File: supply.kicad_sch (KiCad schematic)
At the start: 98 parts, among them IC12 74HC00PW, IC13 SN74LVC1G126DCKR, IC4 TPS7A0518PDBVT, J12 533980471, T3 BSS138APW, U1 LM3671MF-3.3/NOPB, U2 LM62440-Q1, U3 SN74LXC1T45DBVR, U5 LM3671MF-3.3/NOPB, U6 SIC477ED-T1-GE3

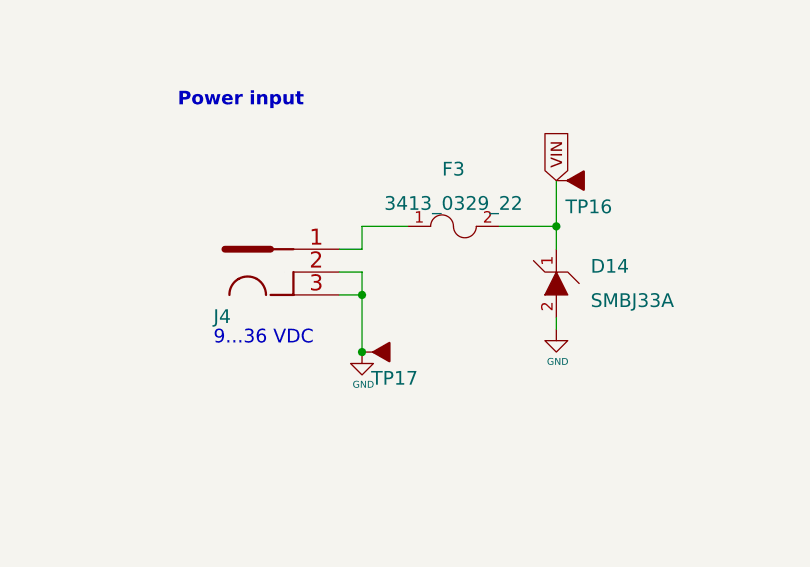
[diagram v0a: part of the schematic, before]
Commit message: WIP: Re-design base board
1. change to more common connector from JLC
2. add WIFI M.2 Key-E connector
3. add USB Hub which contained in nVidia version board
4. change DC connecotor to XT30
5. change USB Mico-B to USB Type C
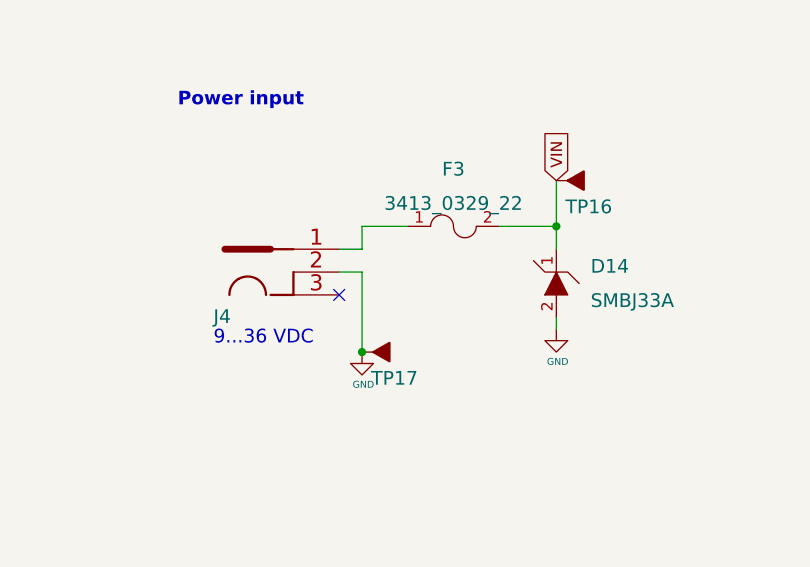
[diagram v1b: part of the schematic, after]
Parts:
- J4: footprint jetson-nano-baseboard-footprints:DC_SOCKET -> JLC_Footprint:CONN-TH_XT30PW-M
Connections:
- net GND: no longer J4.3
- no-connect marks 3 -> 4
